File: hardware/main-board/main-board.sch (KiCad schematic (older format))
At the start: 0 parts

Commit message: Added some sheets and more components to the main board schematics
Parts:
- added C?: 0.1uF, symbol Device:C
- added J?: USB_A, symbol Connector:USB_A
- added J?: NHD OLED Connector, Connector_PinHeader_2.54mm:PinHeader_1x20_P2.54mm_Vertical, symbol Connector_Generic:Conn_01x20
- added LS?: Speaker_Crystal, symbol Device:Speaker_Crystal
- added Q?: 2SC1815, Package_TO_SOT_THT:TO-92_Inline, symbol Transistor_BJT:2SC1815
- added R?: 47K, symbol Device:R
- added R?: 10K, symbol Device:R
- added R?: 1K, symbol Device:R
- added U?: STM32F411RETx, Package_QFP:LQFP-64_10x10mm_P0.5mm, symbol MCU_ST_STM32F4:STM32F411RETx
- added U?: USBLC6-2SC6, Package_TO_SOT_SMD:SOT-23-6, symbol Power_Protection:USBLC6-2SC6
- added U?: STMPS2141, Package_TO_SOT_SMD:SOT-23-5, symbol Project:STMPS2141
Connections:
- net labels added: +3.3V, +5V, BUZZER, DISP_D~C, DISP_SPI_MOSI, DISP_SPI_SCK, DISP_~CS, DISP_~RES, GND, USB_OVERCURRENT, USB_VBUS_EN
- wire segments 0 -> 64
- no-connect marks 0 -> 4

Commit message: Added some off-board I2C interface elements
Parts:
- added C?: 0.1uF, symbol Device:C
- added J?: Sensor Probe Connector, symbol Connector_Generic:Conn_01x05
- added R? (x4): R, symbol Device:R
- added U?: P82B96, symbol Interface_Expansion:P82B96
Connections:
- net labels added: EXT_I2C_SCA, EXT_I2C_SDA, SENSOR_BUTTON
- wire segments 64 -> 99
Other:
- note added: "Connector and\npinout TBD"
- moved on the sheet: J?, LS?, Q?

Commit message: Starting to put main board MCU components in place
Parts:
- removed C? (x2): 0.1uF, symbol Device:C
- removed J?: USB_A, symbol Connector:USB_A
- removed J?: Sensor Probe Connector, symbol Connector_Generic:Conn_01x05
- removed R?: 47K, symbol Device:R
- removed R?: 10K, symbol Device:R
- removed R? (x4): R, symbol Device:R
- removed U?: USBLC6-2SC6, Package_TO_SOT_SMD:SOT-23-6, symbol Power_Protection:USBLC6-2SC6
- removed U?: STMPS2141, Package_TO_SOT_SMD:SOT-23-5, symbol Project:STMPS2141
- removed U?: P82B96, symbol Interface_Expansion:P82B96
- added C? (x2): 8pF, symbol Device:C_Small
- added C? (x7): 0.1uF, symbol Device:C_Small
- added C?: 1uF, symbol Device:C_Small
- added C?: 10 uF, symbol Device:C_Small
- added C?: 4.7uF, Capacitor_SMD:C_1206_3216Metric, symbol Device:C_Small
- added J?: STDC14, lib_fp:Samtec_FTSH-107-01-L-DV-K-A_2x07_P1.27mm, symbol Project:Conn_ST_STDC14
- added L?: 600 Ohm, Inductor_SMD:L_0603_1608Metric, symbol Device:L_Small
- added R?: 10K, symbol Device:R_Small
- added U?: M24M01-RMN, Package_SO:SOIC-8_3.9x4.9mm_P1.27mm, symbol Project:M24M01-RMN
- added Y?: 16MHz, lib_fp:Crystal_SMD_Kyocera_CX3225GB, symbol Device:Crystal_GND24
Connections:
- net labels added: RESET
- net labels removed: EXT_I2C_SCA, EXT_I2C_SDA, SENSOR_BUTTON, USB_OVERCURRENT, USB_VBUS_EN
- wire segments 99 -> 102
- no-connect marks 4 -> 6
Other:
- note added: "0.1uF caps are for each power pin"
- note added: "Find a suitable SMD transistor\nto drive the speaker, or some\nother driver circuit."
- note added: "VCAP needs\n<1ohm ESR"
- note removed: "Connector and\npinout TBD"
- moved on the sheet: J?, LS?, Q?, U?

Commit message: Added more main board parts and models
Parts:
- added D? (x2): ESDALC6V1W5, lib_fp:SOT323-5L, symbol Project:ESDALC6V1W5
- added R?: 100, symbol Device:R_Small
- LS?: footprint (none) -> lib_fp:PKM22EPPH4001-B0; Description (none) -> AUDIO PIEZO TRANSDUCER 30V TH; Manufacturer (none) -> Murata Electronics; Manufacturer PN (none) -> PKM22EPPH4001-B0; Supplier (none) -> Digi-Key; Supplier PN (none) -> 490-4692-ND
- R?: symbol Device:R -> Device:R_Small
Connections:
- net labels added: BUZZ, ENC_CH1, ENC_CH2, I2C1_SCL, I2C1_SDA, I2C2_SCL, I2C2_SDA, JCLK_SWCLK, JTDI, JTDO_SWO, JTMS_SWDIO, KEY_~INT, RELAY_ENLG, RELAY_SFLT, SENSOR_~INT, USART1_RX, USART1_TX, USB_DRIVE_VBUS, USB_OTG_FS_DM, USB_OTG_FS_DP, USB_VBUS_OC
- wire segments 102 -> 151
- no-connect marks 6 -> 9
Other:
- note added: "Can swap connections on ESD\nprotection to optimize routing"
- note added: "May need 4 GPIOs for LED driver\n(One on a TIM channel)"
- moved on the sheet: C?, J?, U?, Y?

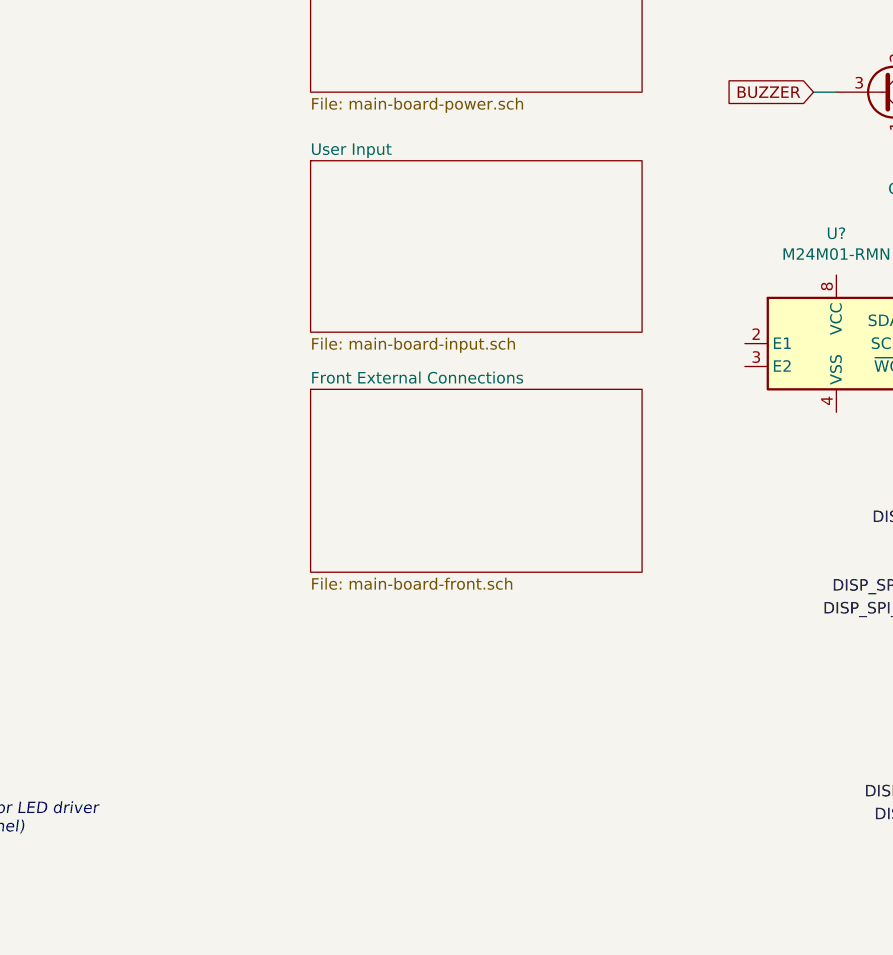
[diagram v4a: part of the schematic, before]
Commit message: More work on main board input and panel connection sheets
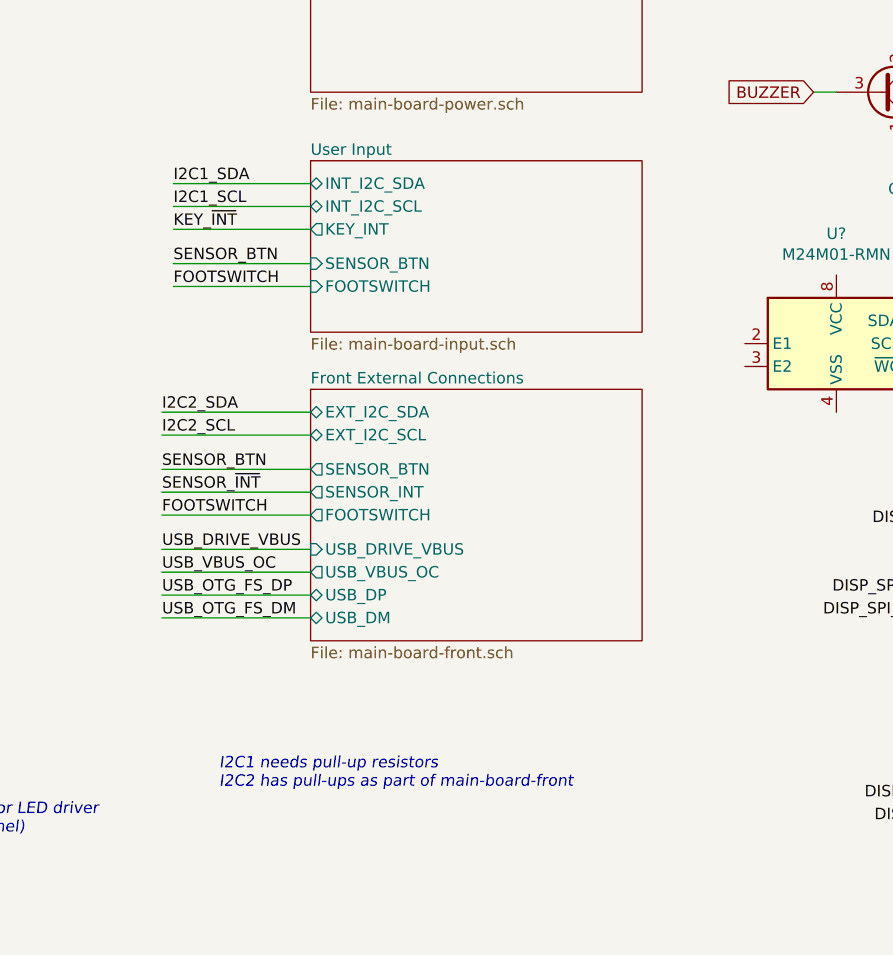
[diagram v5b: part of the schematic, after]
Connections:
- net labels added: FOOTSWITCH, SENSOR_BTN
- wire segments 151 -> 165
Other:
- note added: "I2C1 needs pull-up resistors\nI2C2 has pull-ups as part of main-board-front"
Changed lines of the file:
@@
 F0 "User Input" 50
 F1 "main-board-input.sch" 50
+F2 "INT_I2C_SDA" B L 6500 1850 50
+F3 "INT_I2C_SCL" B L 6500 1950 50
+F4 "SENSOR_BTN" I L 6500 2200 50
+F5 "FOOTSWITCH" I L 6500 2300 50
+F6 "KEY_INT" O L 6500 2050 50
 $EndSheet
 $Comp
@@
 DISP_~CS
 $Sheet
-S 6500 2750 1450 800
+S 6500 2750 1450 1100
 U 5FA19AFF
 F0 "Front External Connections" 50
 F1 "main-board-front.sch" 50
+F2 "EXT_I2C_SDA" B L 6500 2850 50
+F3 "EXT_I2C_SCL" B L 6500 2950 50
+F4 "SENSOR_BTN" O L 6500 3100 50
+F5 "SENSOR_INT" O L 6500 3200 50
+F6 "FOOTSWITCH" O L 6500 3300 50
+F7 "USB_DRIVE_VBUS" I L 6500 3450 50
+F8 "USB_VBUS_OC" O L 6500 3550 50
+F9 "USB_DP" B L 6500 3650 50
+F10 "USB_DM" B L 6500 3750 50
 $EndSheet
 $Comp
@@
 Can swap connections on ESD\nprotection to optimize routing
 NoConn ~ 1700 6050
+Text Label 5850 2950 0    50   ~ 0
+I2C2_SCL
+Text Label 5850 2850 0    50   ~ 0
+I2C2_SDA
+Text Label 5850 3200 0    50   ~ 0
+SENSOR_~INT
+Text Label 5850 3750 0    50   ~ 0
+USB_OTG_FS_DM
+Text Label 5850 3650 0    50   ~ 0
+USB_OTG_FS_DP
+Text Label 5850 3450 0    50   ~ 0
+USB_DRIVE_VBUS
+Text Label 5850 3550 0    50   ~ 0
+USB_VBUS_OC
+Wire Wire Line
+	6500 2850 5850 2850
+Wire Wire Line
+	5850 2950 6500 2950
+Wire Wire Line
+	5850 3200 6500 3200
+Wire Wire Line
+	6500 3450 5850 3450
+Wire Wire Line
+	5850 3550 6500 3550
+Wire Wire Line
+	5850 3650 6500 3650
+Wire Wire Line
+	5850 3750 6500 3750
+Text Label 5900 2200 0    50   ~ 0
+SENSOR_BTN
+Text Label 5900 2300 0    50   ~ 0
+FOOTSWITCH
+Text Label 5850 3100 0    50   ~ 0
+SENSOR_BTN
+Text Label 5850 3300 0    50   ~ 0
+FOOTSWITCH
+Wire Wire Line
+	6500 2200 5900 2200
+Wire Wire Line
+	5900 2300 6500 2300
+Wire Wire Line
+	5850 3300 6500 3300
+Wire Wire Line
+	5850 3100 6500 3100
+Text Label 5900 1850 0    50   ~ 0
+I2C1_SDA
+Text Label 5900 1950 0    50   ~ 0
+I2C1_SCL
+Wire Wire Line
+	5900 1950 6500 1950
+Wire Wire Line
+	5900 1850 6500 1850
+Text Label 5900 2050 0    50   ~ 0
+KEY_~INT
+Wire Wire Line
+	5900 2050 6500 2050
+Text Notes 6100 4500 0    50   Italic 0
+I2C1 needs pull-up resistors\nI2C2 has pull-ups as part of main-board-front
 $EndSCHEMATC

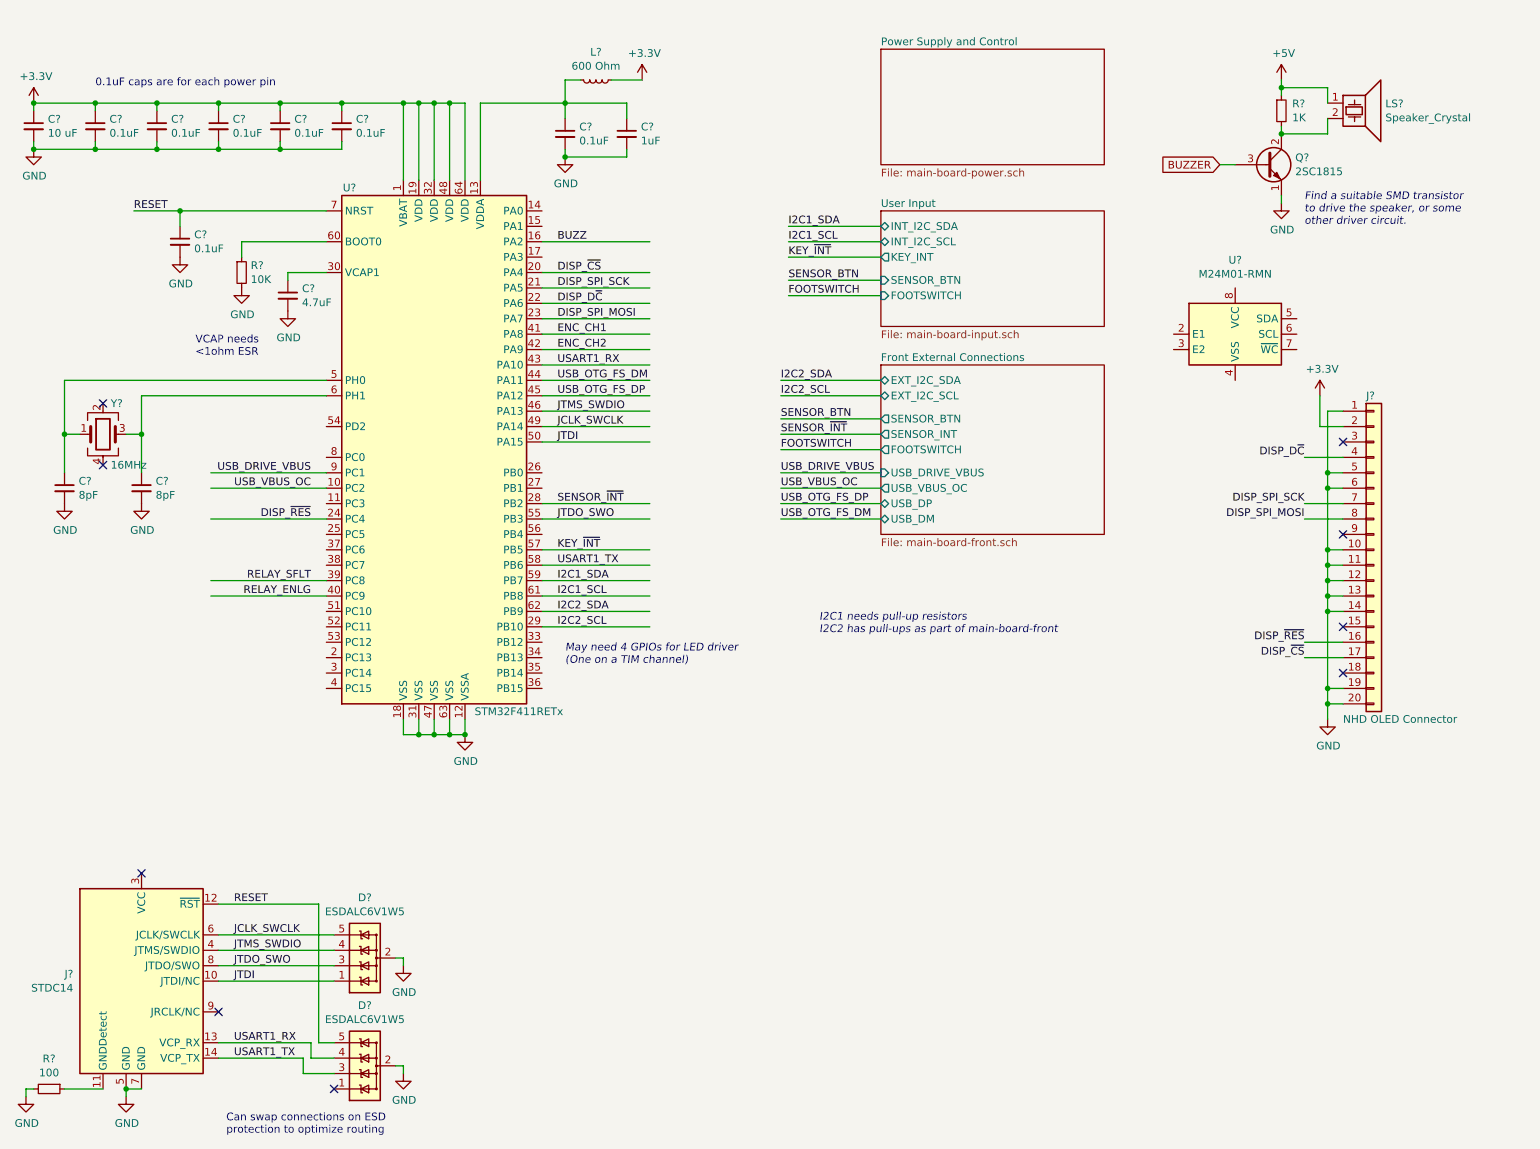
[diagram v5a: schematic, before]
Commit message: Power input and buzzer driver schematic work
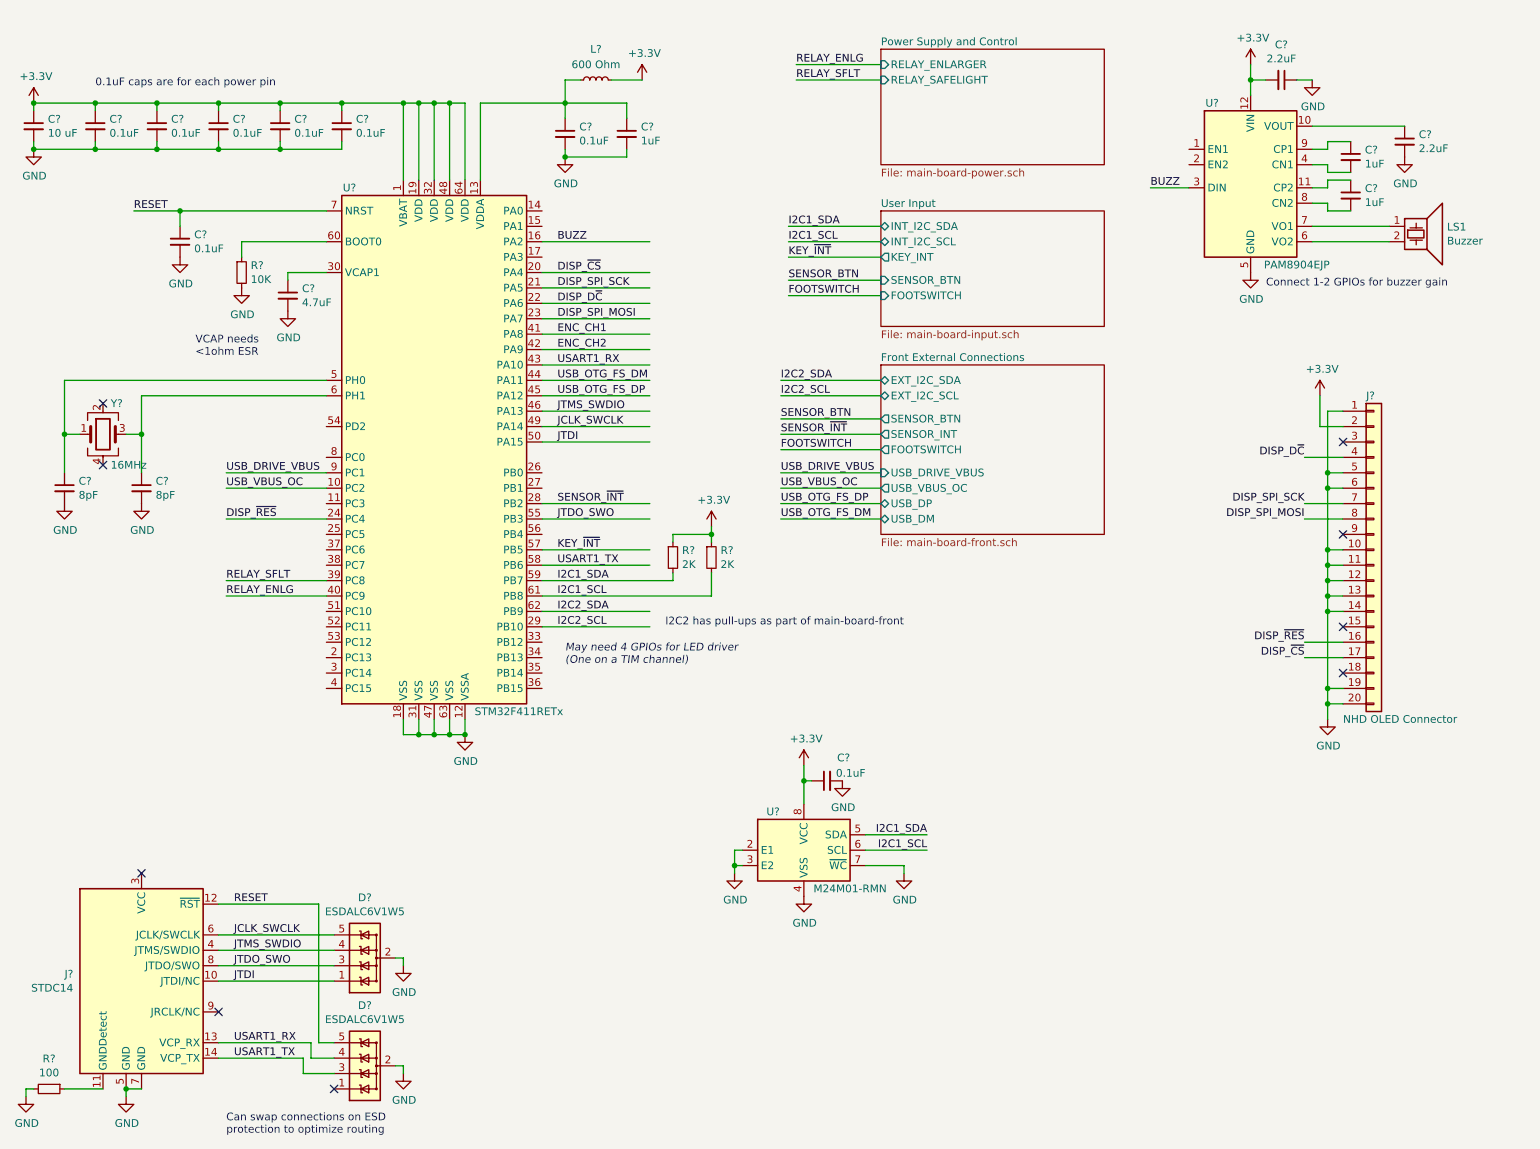
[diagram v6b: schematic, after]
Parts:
- removed LS?: Speaker_Crystal, lib_fp:PKM22EPPH4001-B0, symbol Device:Speaker_Crystal
- removed Q?: 2SC1815, Package_TO_SOT_THT:TO-92_Inline, symbol Transistor_BJT:2SC1815
- removed R?: 1K, symbol Device:R_Small
- added C?: 0.1uF, symbol Device:C_Small
- added C? (x2): 2.2uF, Capacitor_SMD:C_0805_2012Metric, symbol Device:C_Small
- added C? (x2): 1uF, Capacitor_SMD:C_0603_1608Metric, symbol Device:C_Small
- added LS1: Buzzer, lib_fp:PKM22EPPH4001-B0, symbol Device:Speaker_Crystal
- added R? (x2): 2K, symbol Device:R_Small
- added U?: PAM8904EJP, lib_fp:U-QFN3030-12_Type-A, symbol Project:PAM8904EJP
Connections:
- net labels removed: +5V, BUZZER
- wire segments 165 -> 195
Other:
- note added: "Connect 1-2 GPIOs for buzzer gain"
- note added: "I2C2 has pull-ups as part of main-board-front"
- note removed: "Find a suitable SMD transistor\nto drive the speaker, or some\nother driver circuit."
- note removed: "I2C1 needs pull-up resistors\nI2C2 has pull-ups as part of main-board-front"
- moved on the sheet: L?, U?
